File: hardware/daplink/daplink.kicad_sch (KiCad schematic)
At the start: 33 parts, among them J1 Conn_01x04, J2 Conn_01x05, J3 Conn_01x05, P1 USB_C_Plug_USB2.0, U1 AMS1117-3.3, U2 STM32F103CBTx, Y1 8MHz

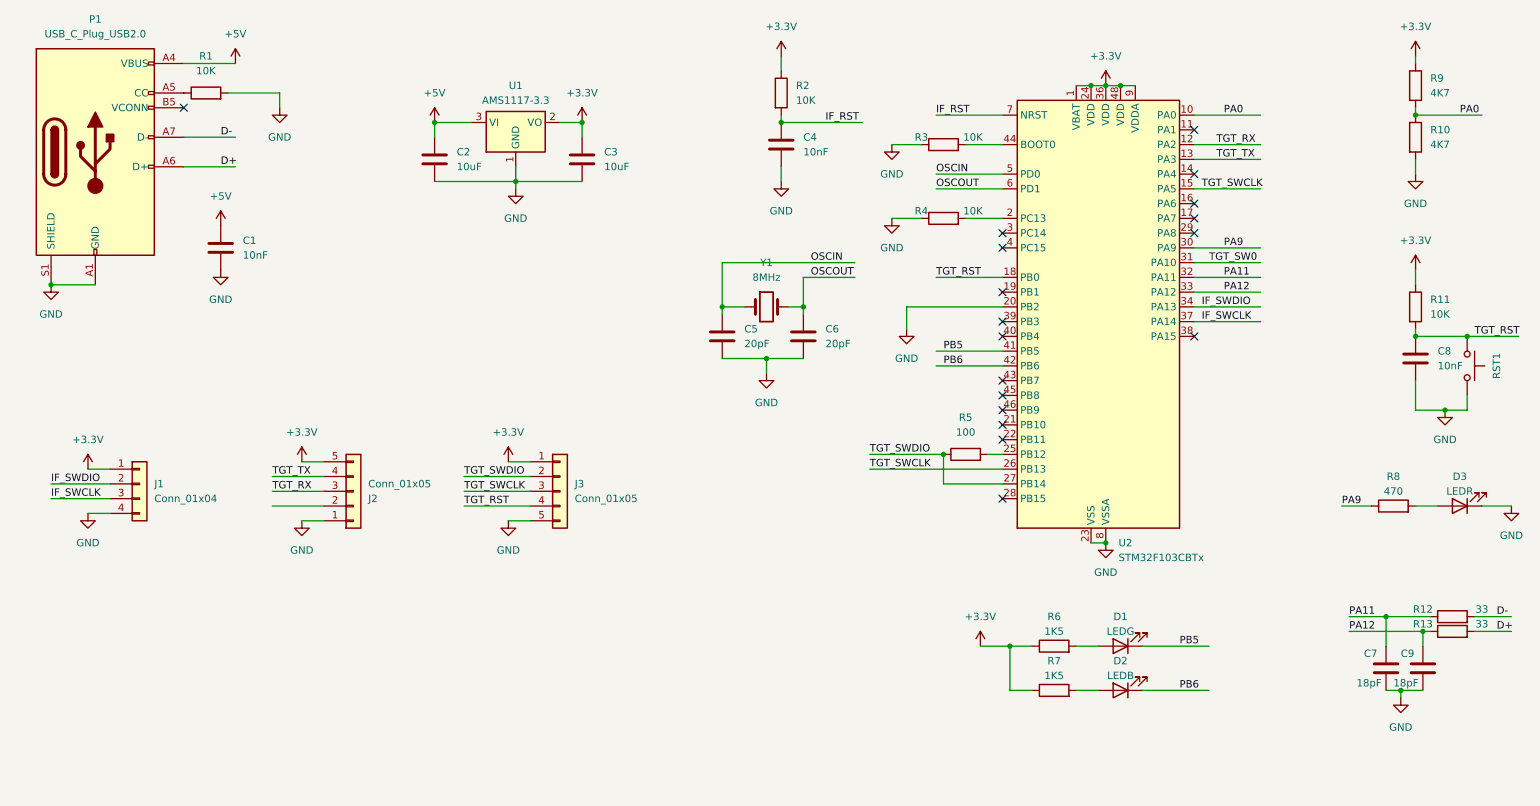
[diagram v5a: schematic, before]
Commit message: fix(hw/usb): d+ pull up and support usb-c flip
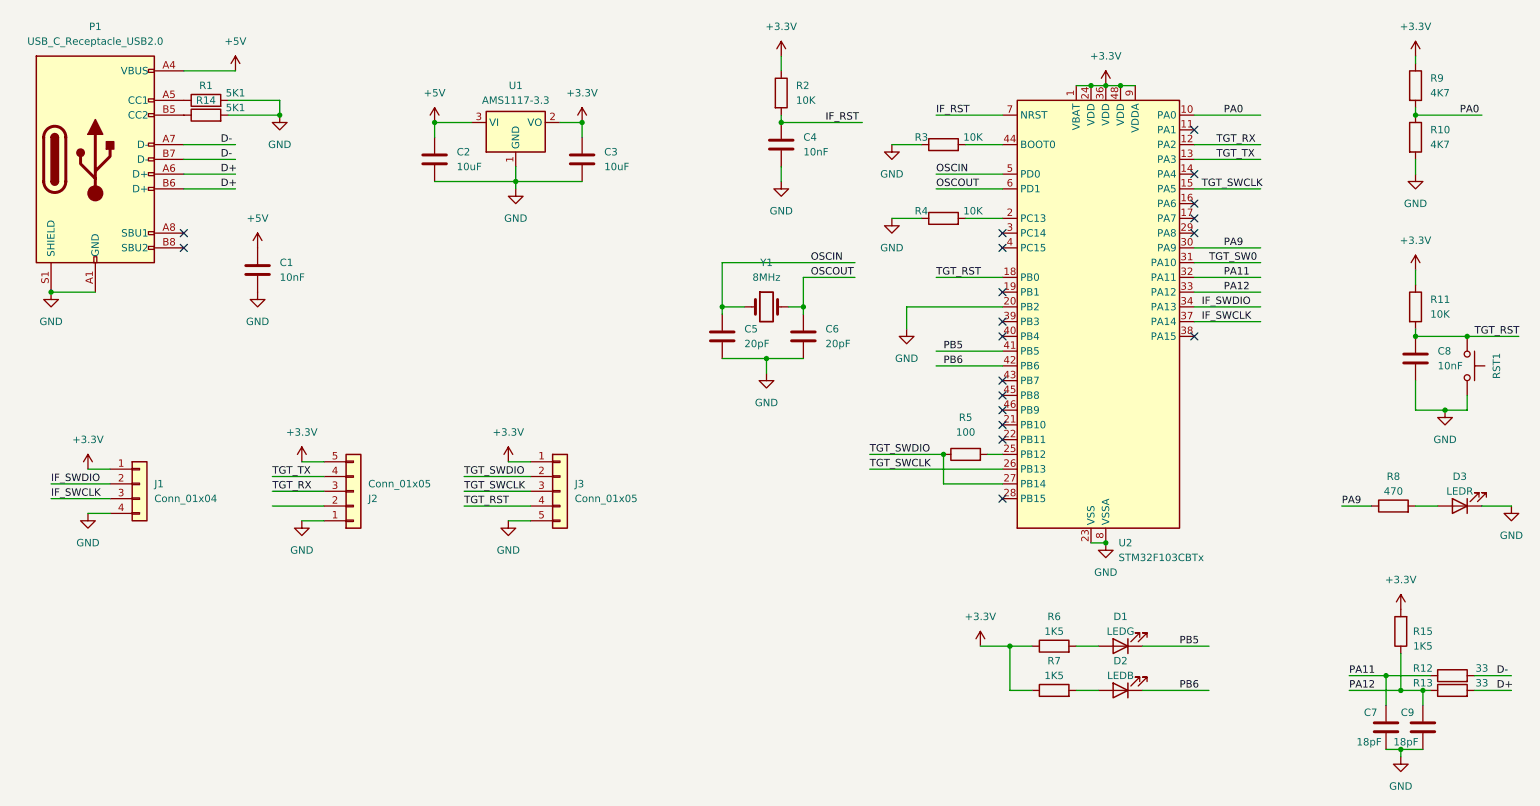
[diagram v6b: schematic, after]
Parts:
- removed P1: USB_C_Plug_USB2.0, Connector_USB:USB_C_Receptacle_GCT_USB4105-xx-A_16P_TopMnt_Horizontal, symbol Connector:USB_C_Plug_USB2.0
- added P1: USB_C_Receptacle_USB2.0, Connector_USB:USB_C_Receptacle_GCT_USB4105-xx-A_16P_TopMnt_Horizontal, symbol Connector:USB_C_Receptacle_USB2.0
- added R14: 5K1, Resistor_SMD:R_0603_1608Metric_Pad0.98x0.95mm_HandSolder, symbol Device:R
- added R15: 1K5, Resistor_SMD:R_0603_1608Metric_Pad0.98x0.95mm_HandSolder, symbol Device:R
- R1: value 10K -> 5K1
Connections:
- net +3.3V: now also R15.2
- net +5V: now also P1.A4 (VBUS), P1.A9 (VBUS), P1.B4 (VBUS), P1.B9 (VBUS)
- net D+: now also P1.A6 (D+), P1.B6 (D+)
- net D-: now also P1.A7 (D-), P1.B7 (D-)
- net GND: now also P1.A1 (GND), P1.A12 (GND), P1.B1 (GND), P1.B12 (GND), P1.S1 (SHIELD), R14.2
- net PA12: now also R15.1
- net at R1.1: now also P1.A5 (CC1)
- new net: P1.B5 (CC2), R14.1
- no-connect marks 18 -> 19
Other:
- moved on the sheet: C1, C7, C9, R12, R13

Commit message: refactor(hw/usb): modify board outline
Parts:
- R15: JLCPCB C23140 -> C22843
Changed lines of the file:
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@@
       (effects (font (size 1.27 1.27)) hide)
     )
-    (property "JLCPCB" "C23140" (at 260.35 125.73 0)
+    (property "JLCPCB" "C22843" (at 260.35 125.73 0)
       (effects (font (size 1.27 1.27)) hide)
     )

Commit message: fix(hw/usb): fix part number
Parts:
- R1, R14: JLCPCB C25804 -> C23186
- R5: JLCPCB C23162 -> C22775
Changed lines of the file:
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@@
       (effects (font (size 1.27 1.27)) hide)
     )
-    (property "JLCPCB" "C23162" (at 185.42 95.25 0)
+    (property "JLCPCB" "C22775" (at 185.42 95.25 0)
       (effects (font (size 1.27 1.27)) hide)
     )
@@
       (effects (font (size 1.27 1.27)) hide)
     )
-    (property "JLCPCB" "C25804" (at 54.61 34.29 0)
+    (property "JLCPCB" "C23186" (at 54.61 34.29 0)
       (effects (font (size 1.27 1.27)) hide)
     )
@@
       (effects (font (size 1.27 1.27)) hide)
     )
-    (property "JLCPCB" "C25804" (at 54.61 36.83 0)
-      (effects (font (size 1.27 1.27)) hide)
-    )
+    (property "JLCPCB" "C23186" (at 54.61 36.83 0)
+      (effects (font (size 1.27 1.27)) hide)
+    )
